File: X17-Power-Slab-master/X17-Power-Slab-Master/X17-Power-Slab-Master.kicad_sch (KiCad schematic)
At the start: 17 parts, among them J1 Conn_01x05, J2 ET60S-D04-3-08-D04-X-R1-S, Q1 NMOS, U1 AZ1117IH-3.3TRG1, U4 STM32F091CCTx, Y1 Crystal

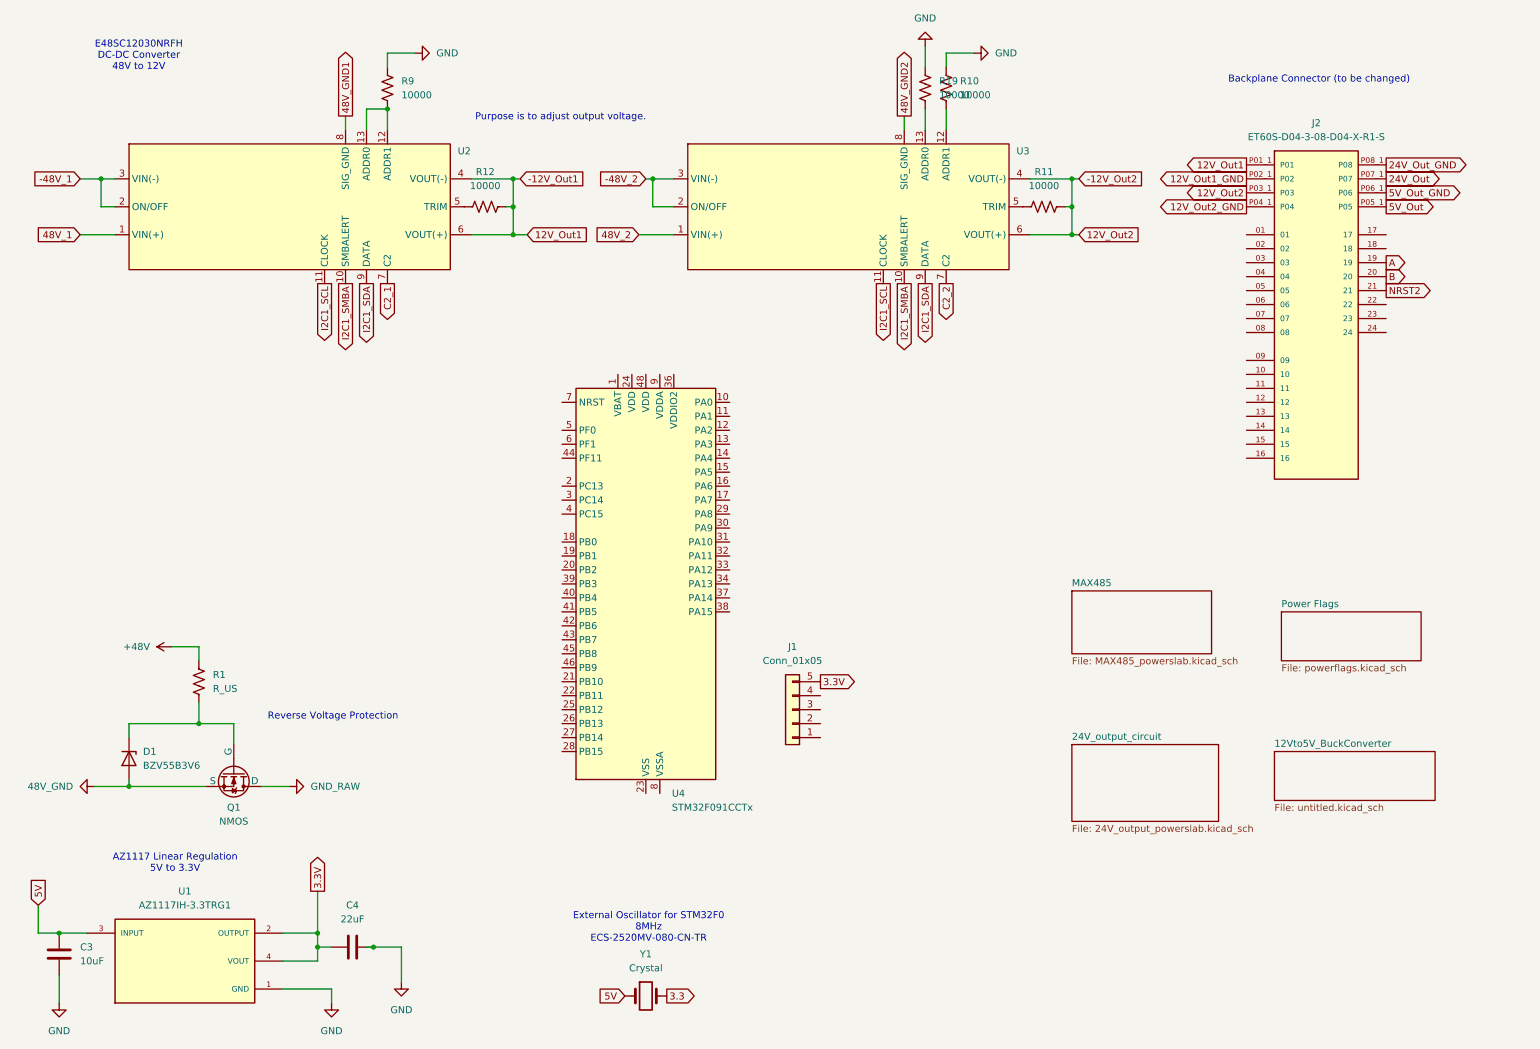
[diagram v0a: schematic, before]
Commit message: STM32 Pinout
Complete STM32 pinout added without connector (need to find model and download)
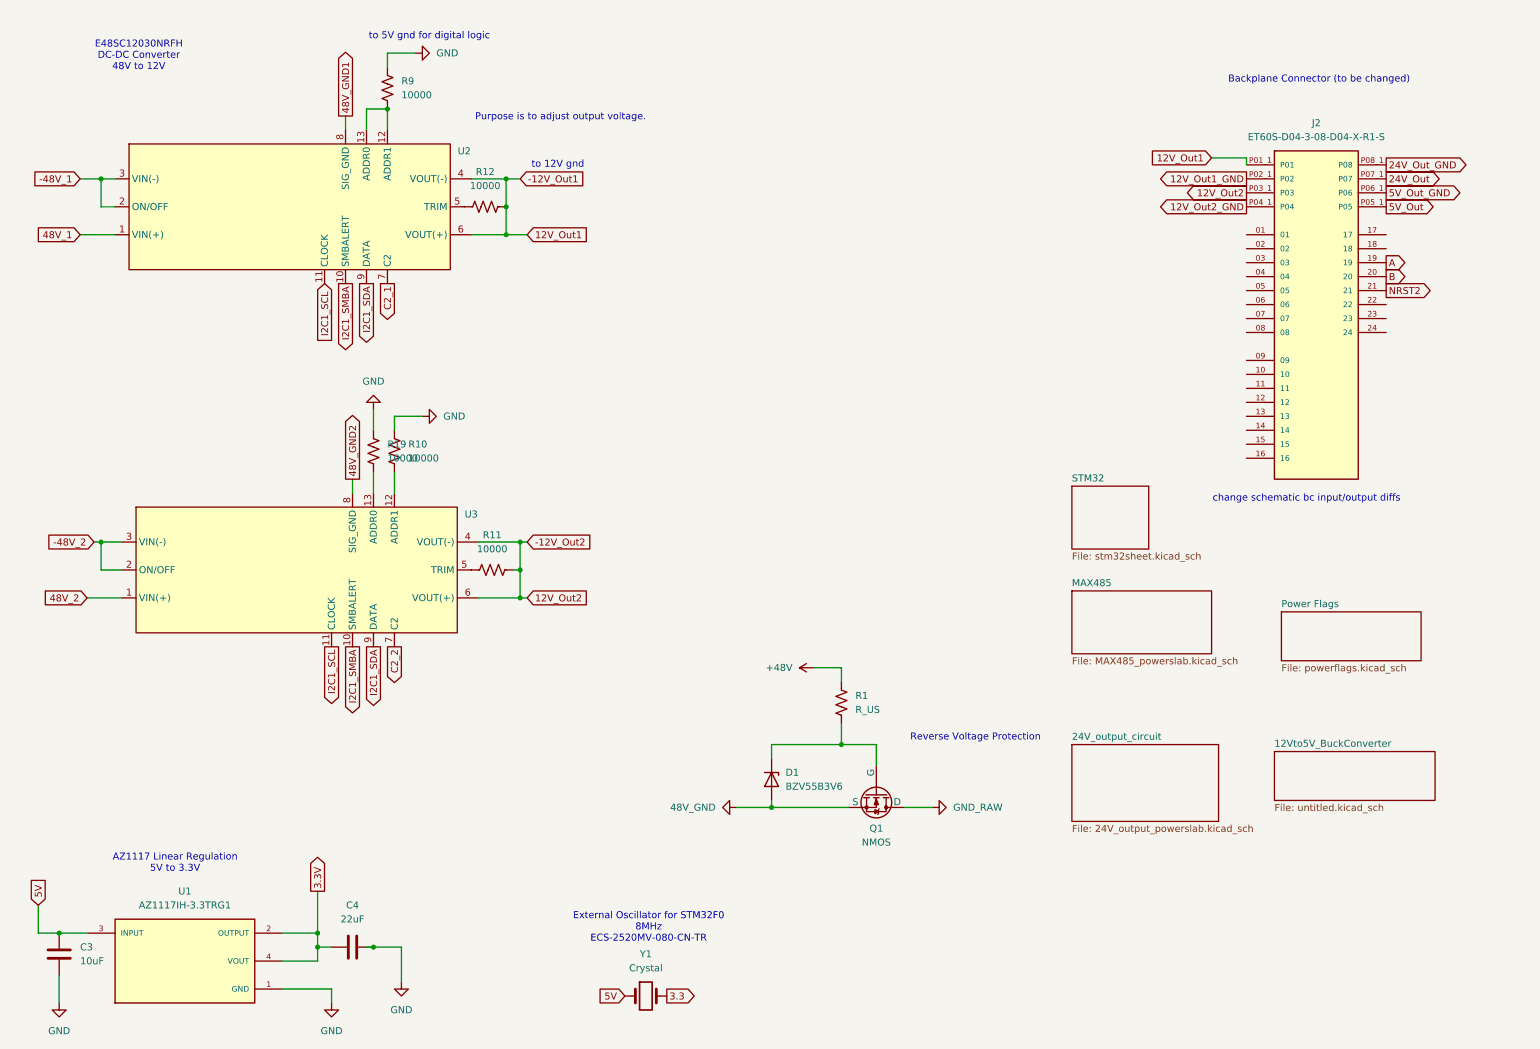
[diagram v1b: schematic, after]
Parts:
- removed J1: Conn_01x05, symbol Connector_Generic:Conn_01x05
- removed U4: STM32F091CCTx, Package_QFP:LQFP-48_7x7mm_P0.5mm, symbol MCU_ST_STM32F0:STM32F091CCTx
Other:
- added sheet STM32 (stm32sheet.kicad_sch)
- note added: "change schematic bc input/output diffs"
- note added: "to 12V gnd"
- note added: "to 5V gnd for digital logic"
- moved on the sheet: D1, Q1, R1, R10, R11, R19, U3

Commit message: Schematic Updates
#SlayedTheDayAway
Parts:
- removed Y1: Crystal, symbol Device:Crystal
- added J3: 796636-6, footprints:CON6_P5MM_VER_TERM-BLK_TYC, symbol Tether Connection:796636-6
- added R23, R24, R25: 10k, symbol Device:R_US
- R10, R11, R12, R19, R9: value 10000 -> 10k
- U3: footprint (none) -> E48SC12030NRFH_Footprint:E48SC12030NRFH_Footprint
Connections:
- net -48V_2 is gone; now on net -48V: U3.2 (ON/OFF), U3.3 (VIN(-))
- net 48V_1 is gone; now on net 48V: U2.1 (VIN(+))
- net 48V_2 is gone; now on net 48V: U3.1 (VIN(+))
- net B is gone; now on net 5V: J2.20
- net 48V_GND: now also J2.07, J2.08
- net GND: no longer R10.1, R19.1, R9.1, U1.1 (GND)
- net NRST2: now also J2.03; no longer J2.21
- net at R10.2: now also U3.13 (ADDR0); no longer U3.12 (ADDR1)
- net at R9.2, U2.12 (ADDR1): no longer U2.13 (ADDR0)
- net at R11.1, U3.5 (TRIM): now also R24.1
- net at R12.1, U2.5 (TRIM): now also R23.1
- net at R19.2: now also U2.13 (ADDR0); no longer U3.13 (ADDR0)
- net A+: now reaches J2.01
- net A-: now reaches J2.02
- net 48V: now reaches J2.05
- net 48V: now also J2.06
- net -48V_1 renamed -48V
- net A: no longer names the net of J2.19
- net P01 renamed 12V_GND1
- net 12V_GND1: no longer U2.6 (VOUT(+))
- net P02 renamed 12V_GND2
- net 12V_GND2: now also R11.2, U3.4 (VOUT(-))
- removed net P03: J2.P03_1 (P03), R11.2, U3.4 (VOUT(-)), U3.6 (VOUT(+))
- net P04 renamed 12V_2
- net 12V_2: now also U3.6 (VOUT(+)), R24.2
- net P05: no longer names the net of J2.P05_1 (P05)
- net P06: no longer names the net of J2.P06_1 (P06)
- net P07: no longer names the net of J2.P07_1 (P07)
- net P08: no longer names the net of J2.P08_1 (P08)
- new net: R25.2, U3.12 (ADDR1)
- new net 12V_1: J2.P03_1 (P03), R23.2, U2.6 (VOUT(+))
- new net 5V_GND: J2.21, R10.1, R19.1, R25.1, R9.1, U1.1 (GND)
- no-connect marks 0 -> 19
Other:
- note added: "A is A+ B is A-"
- note added: "Near the STM for its voltage"
- note removed: "External Oscillator for STM32F0 8MHz ECS-2520MV-080-CN-TR"
- moved on the sheet: R12

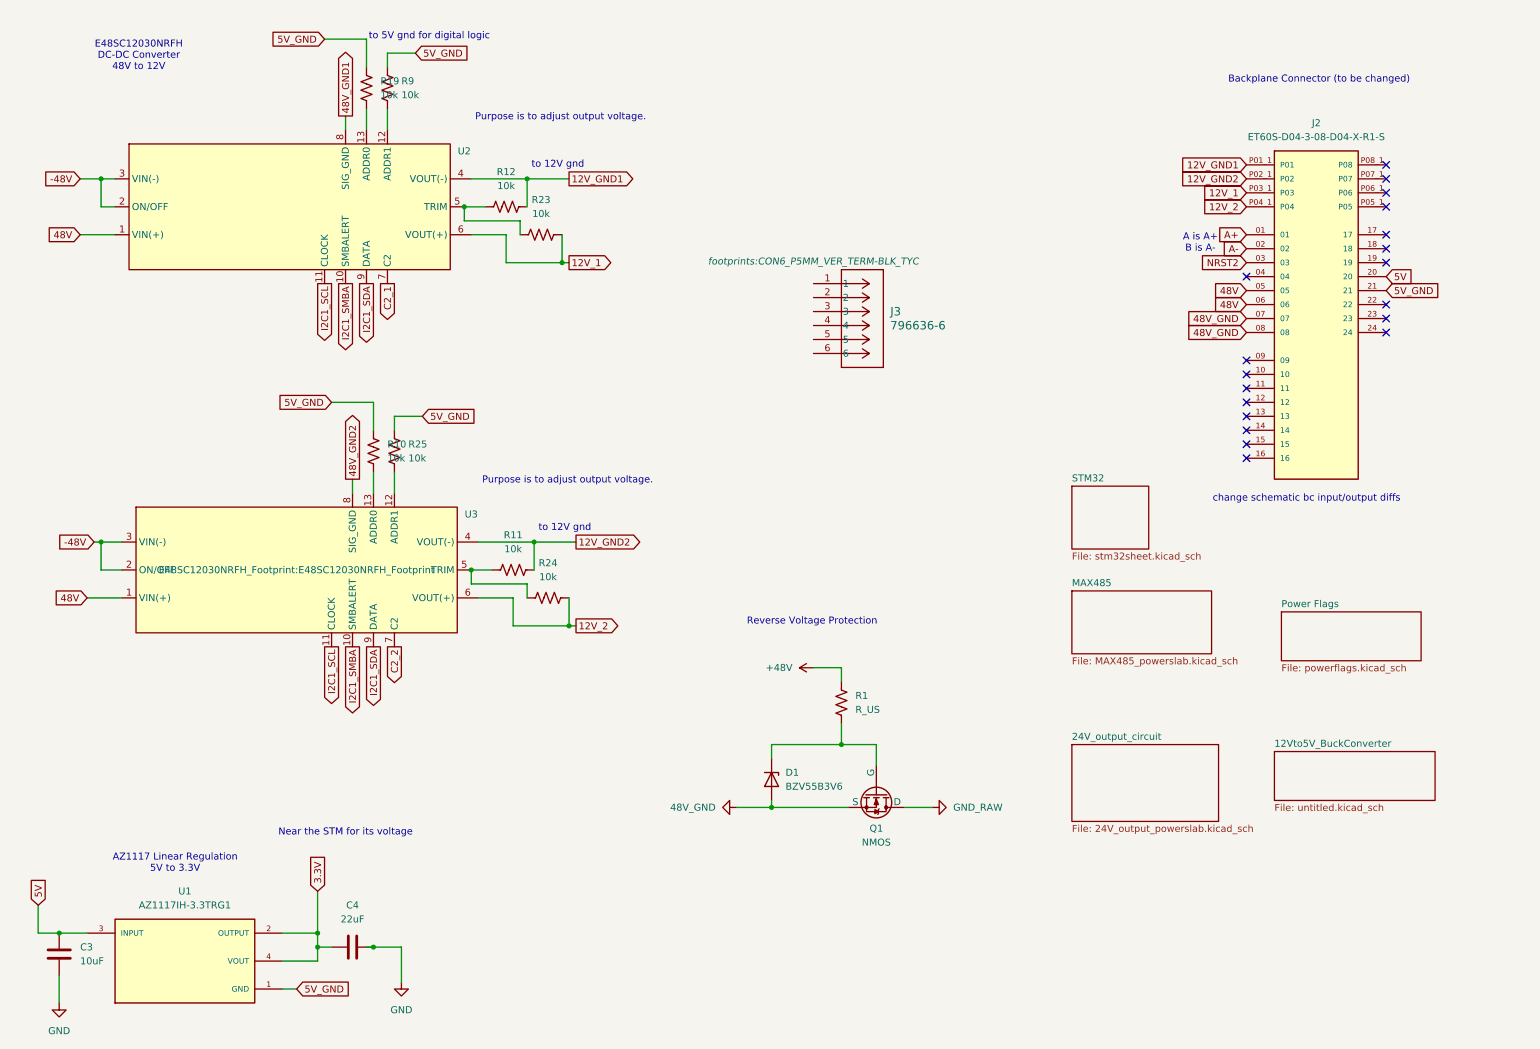
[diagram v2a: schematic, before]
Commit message: Schematic Full Update
Probs can start pacing after this.
Diode on RVP changed,
Button changed
Reverse voltage updated
Symbols updated to remove DRCs
GNDs changed
Connector updated
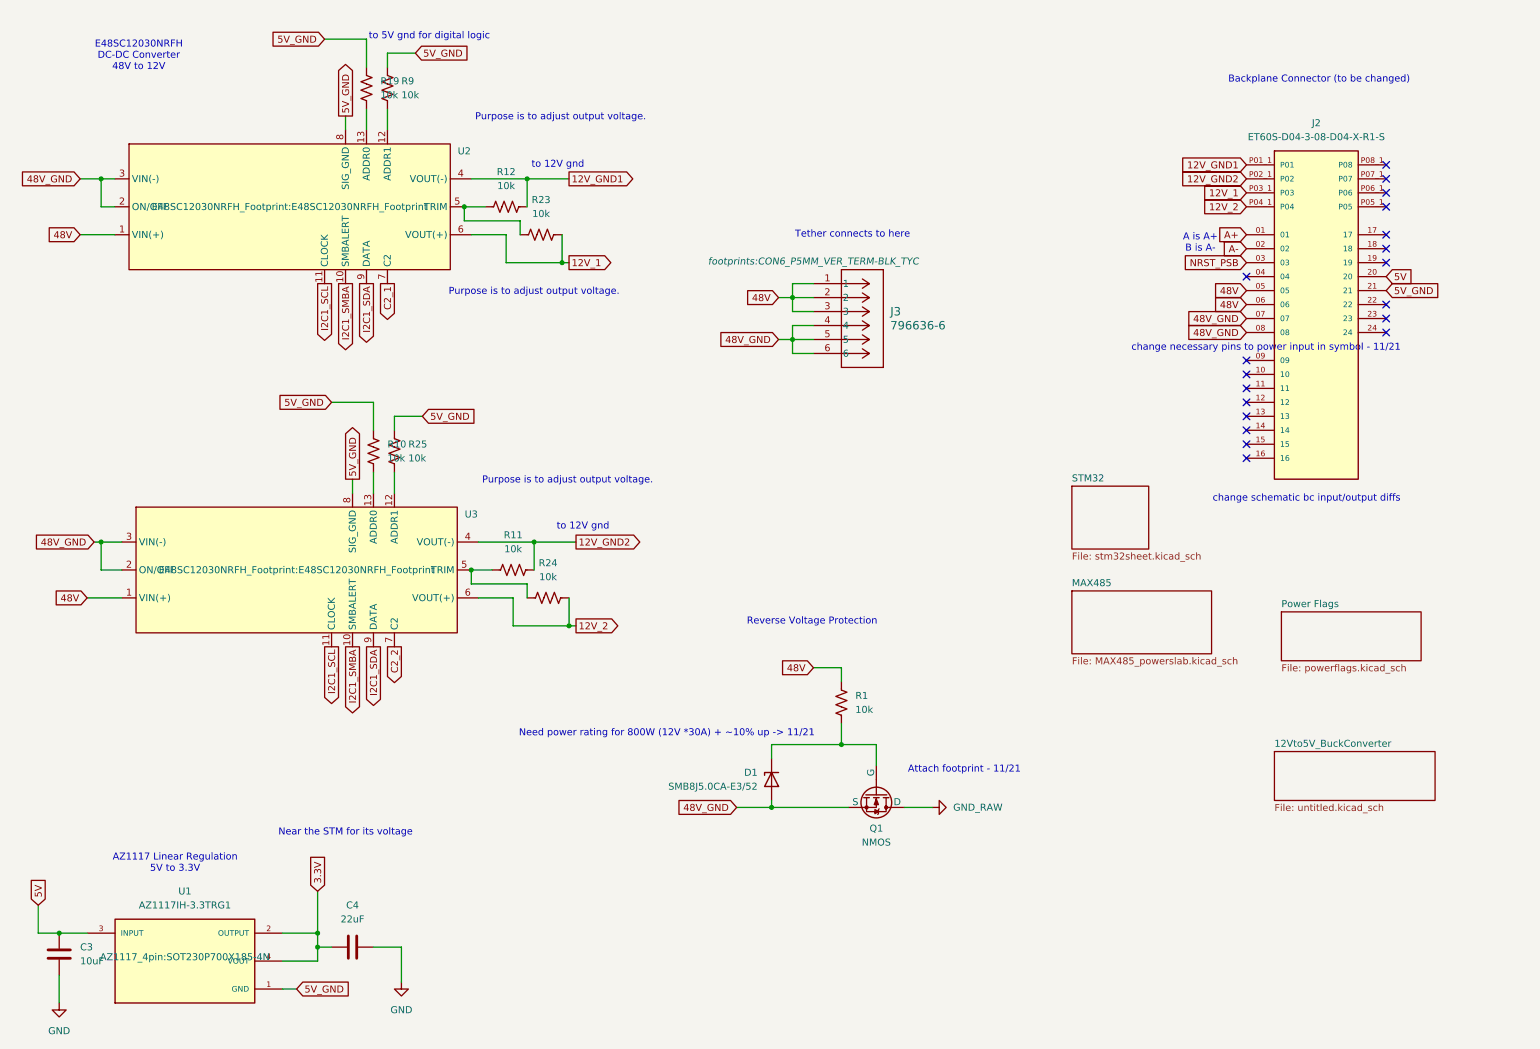
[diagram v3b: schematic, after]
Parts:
- C3, C4: footprint (none) -> Capacitor_SMD:C_0603_1608Metric_Pad1.08x0.95mm_HandSolder
- D1: value BZV55B3V6 -> SMB8J5.0CA-E3/52; footprint Diode_SMD:D_MiniMELF -> Diode_SMD:D_1210_3225Metric_Pad1.42x2.65mm_HandSolder
- Q1: footprint (none) -> Reverse Voltage Protection:TO254P1524X483-4
- R1: value R_US -> 10k; footprint (none) -> Resistor_SMD:R_0603_1608Metric_Pad0.98x0.95mm_HandSolder
- R10, R11, R12, R19, R23, R24, R25, R9: footprint (none) -> Resistor_SMD:R_0603_1608Metric_Pad0.98x0.95mm_HandSolder
- U1: footprint AZ1117IH-3.3TRG1:SOT230P700X185-4N -> AZ1117_4pin:SOT230P700X185-4N
- U2: footprint (none) -> E48SC12030NRFH_Footprint:E48SC12030NRFH_Footprint
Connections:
- net +48V is gone; now on net 48V: R1.1
- net -48V is gone; now on net 48V_GND: U2.2 (ON/OFF), U2.3 (VIN(-)), U3.2 (ON/OFF), U3.3 (VIN(-))
- net 48V_GND1 is gone; now on net 5V_GND: U2.8 (SIG_GND)
- net 48V_GND2 is gone; now on net 5V_GND: U3.8 (SIG_GND)
- net 48V: now also J3.1, J3.2, J3.3
- net 48V_GND: now also J3.4, J3.5, J3.6
- net NRST2 renamed NRST_PSB
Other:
- removed sheet 24V_output_circuit
- note added: "Attach footprint - 11/21"
- note added: "Need power rating for 800W (12V *30A) + ~10% up -> 11/21"
- note added: "Tether connects to here"
- note added: "change necessary pins to power input in symbol - 11/21"
- moved on the sheet: D1
